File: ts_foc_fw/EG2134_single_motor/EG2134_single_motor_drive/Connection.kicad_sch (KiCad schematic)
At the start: 3 parts, among them CN1 XT30PW-M, CN2 WAFER-GH1.25-10PWB, U2 MR30PW-M30.G.Y

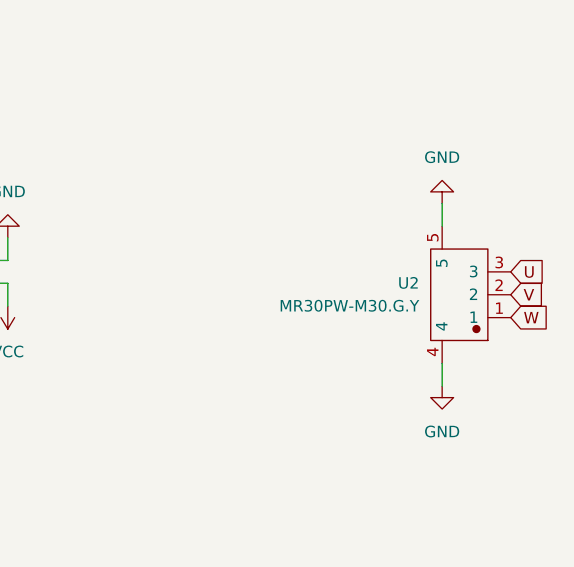
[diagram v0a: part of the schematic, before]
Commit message: PCB布局完成，等待布线
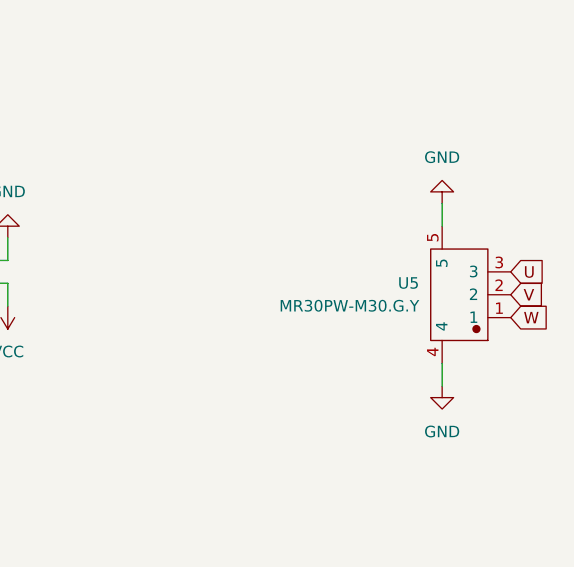
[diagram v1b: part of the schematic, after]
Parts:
- renumbered U2 to U5
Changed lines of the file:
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@@
 		(dnp no)
 		(fields_autoplaced yes)
-		(property "Reference" "#PWR09"
+		(property "Reference" "#PWR031"
 			(at 77.47 69.85 0)
 			(effects
@@
 			(project ""
 				(path "/a69a3027-f6f2-4dc7-8446-d1a07c691b27/9b51b494-1b93-4e31-bc4e-8becface2ca1"
-					(reference "#PWR09")
+					(reference "#PWR031")
 					(unit 1)
 				)
@@
 		(dnp no)
 		(fields_autoplaced yes)
-		(property "Reference" "#PWR017"
+		(property "Reference" "#PWR038"
 			(at 138.43 72.39 0)
 			(effects
@@
 			(project "EG2134_single_motor_drive"
 				(path "/a69a3027-f6f2-4dc7-8446-d1a07c691b27/9b51b494-1b93-4e31-bc4e-8becface2ca1"
-					(reference "#PWR017")
+					(reference "#PWR038")
 					(unit 1)
 				)
@@
 		(dnp no)
 		(fields_autoplaced yes)
-		(property "Reference" "#PWR015"
+		(property "Reference" "#PWR034"
 			(at 88.9 129.54 0)
 			(effects
@@
 			(project "EG2134_single_motor_drive"
 				(path "/a69a3027-f6f2-4dc7-8446-d1a07c691b27/9b51b494-1b93-4e31-bc4e-8becface2ca1"
-					(reference "#PWR015")
+					(reference "#PWR034")
 					(unit 1)
 				)
@@
 		(dnp no)
 		(fields_autoplaced yes)
-		(property "Reference" "#PWR013"
+		(property "Reference" "#PWR032"
 			(at 77.47 86.36 0)
 			(effects
@@
 			(project "EG2134_single_motor_drive"
 				(path "/a69a3027-f6f2-4dc7-8446-d1a07c691b27/9b51b494-1b93-4e31-bc4e-8becface2ca1"
-					(reference "#PWR013")
+					(reference "#PWR032")
 					(unit 1)
 				)
@@
 		(dnp no)
 		(fields_autoplaced yes)
-		(property "Reference" "#PWR011"
+		(property "Reference" "#PWR035"
 			(at 90.17 43.18 0)
 			(effects
@@
 			(project "EG2134_single_motor_drive"
 				(path "/a69a3027-f6f2-4dc7-8446-d1a07c691b27/9b51b494-1b93-4e31-bc4e-8becface2ca1"
-					(reference "#PWR011")
+					(reference "#PWR035")
 					(unit 1)
 				)
@@
 		(dnp no)
 		(fields_autoplaced yes)
-		(property "Reference" "#PWR014"
+		(property "Reference" "#PWR033"
 			(at 77.47 137.16 0)
 			(effects
@@
 			(project "EG2134_single_motor_drive"
 				(path "/a69a3027-f6f2-4dc7-8446-d1a07c691b27/9b51b494-1b93-4e31-bc4e-8becface2ca1"
-					(reference "#PWR014")
+					(reference "#PWR033")
 					(unit 1)
 				)
@@
 		(dnp no)
 		(fields_autoplaced yes)
-		(property "Reference" "#PWR012"
+		(property "Reference" "#PWR036"
 			(at 90.17 53.34 0)
 			(effects
@@
 			(project ""
 				(path "/a69a3027-f6f2-4dc7-8446-d1a07c691b27/9b51b494-1b93-4e31-bc4e-8becface2ca1"
-					(reference "#PWR012")
+					(reference "#PWR036")
 					(unit 1)
 				)
@@
 		(dnp no)
 		(fields_autoplaced yes)
-		(property "Reference" "U2"
+		(property "Reference" "U5"
 			(at 135.89 54.6099 0)
 			(effects
@@
 			(project ""
 				(path "/a69a3027-f6f2-4dc7-8446-d1a07c691b27/9b51b494-1b93-4e31-bc4e-8becface2ca1"
-					(reference "U2")
+					(reference "U5")
 					(unit 1)
 				)
@@
 		(dnp no)
 		(fields_autoplaced yes)
-		(property "Reference" "#PWR016"
+		(property "Reference" "#PWR037"
 			(at 138.43 39.37 0)
 			(effects
@@
 			(project "EG2134_single_motor_drive"
 				(path "/a69a3027-f6f2-4dc7-8446-d1a07c691b27/9b51b494-1b93-4e31-bc4e-8becface2ca1"
-					(reference "#PWR016")
+					(reference "#PWR037")
 					(unit 1)
 				)
@@
 		(dnp no)
 		(fields_autoplaced yes)
-		(property "Reference" "#PWR010"
+		(property "Reference" "#PWR030"
 			(at 77.47 38.1 0)
 			(effects
@@
 			(project "EG2134_single_motor_drive"
 				(path "/a69a3027-f6f2-4dc7-8446-d1a07c691b27/9b51b494-1b93-4e31-bc4e-8becface2ca1"
-					(reference "#PWR010")
-					(unit 1)
-				)
+					(reference "#PWR030")
+					(unit 1)
+				)

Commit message: tongbu
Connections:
- net CS_1 renamed CS1
- net CS_2 renamed CS2
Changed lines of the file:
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@@
+	(wire
+		(pts
+			(xy 90.17 100.33) (xy 86.36 100.33)
+		)
+		(stroke
+			(width 0)
+			(type default)
+		)
+	)
+	(wire
+		(pts
+			(xy 90.17 102.87) (xy 86.36 102.87)
+		)
+		(stroke
+			(width 0)
+			(type default)
+		)
+	)
 	(wire
 		(pts
@@
 	(wire
 		(pts
+			(xy 90.17 107.95) (xy 86.36 107.95)
+		)
+		(stroke
+			(width 0)
+			(type default)
+		)
+	)
+	(wire
+		(pts
+			(xy 90.17 110.49) (xy 86.36 110.49)
+		)
+		(stroke
+			(width 0)
+			(type default)
+		)
+	)
+	(wire
+		(pts
 			(xy 138.43 45.72) (xy 138.43 48.26)
 		)
@@
 		(pts
 			(xy 77.47 130.81) (xy 77.47 128.27)
+		)
+		(stroke
+			(width 0)
+			(type default)
+		)
+	)
+	(wire
+		(pts
+			(xy 90.17 105.41) (xy 86.36 105.41)
 		)
 		(stroke
@@
 		)
 	)
-	(global_label "CS_1"
-		(shape input)
-		(at 86.36 107.95 0)
-		(fields_autoplaced yes)
-		(effects
-			(font
-				(size 1.27 1.27)
-			)
-			(justify left)
-		)
-		(property "Intersheetrefs" "${INTERSHEET_REFS}"
-			(at 94.0018 107.95 0)
+	(global_label "CS1"
+		(shape input)
+		(at 90.17 107.95 0)
+		(fields_autoplaced yes)
+		(effects
+			(font
+				(size 1.27 1.27)
+			)
+			(justify left)
+		)
+		(property "Intersheetrefs" "${INTERSHEET_REFS}"
+			(at 96.8442 107.95 0)
 			(effects
 				(font
@@
 	(global_label "IN_2"
 		(shape input)
-		(at 86.36 102.87 0)
-		(fields_autoplaced yes)
-		(effects
-			(font
-				(size 1.27 1.27)
-			)
-			(justify left)
-		)
-		(property "Intersheetrefs" "${INTERSHEET_REFS}"
-			(at 93.4576 102.87 0)
-			(effects
-				(font
-					(size 1.27 1.27)
-				)
-				(justify left)
-				(hide yes)
-			)
-		)
-	)
-	(global_label "CS_2"
-		(shape input)
-		(at 86.36 110.49 0)
-		(fields_autoplaced yes)
-		(effects
-			(font
-				(size 1.27 1.27)
-			)
-			(justify left)
-		)
-		(property "Intersheetrefs" "${INTERSHEET_REFS}"
-			(at 94.0018 110.49 0)
+		(at 90.17 102.87 0)
+		(fields_autoplaced yes)
+		(effects
+			(font
+				(size 1.27 1.27)
+			)
+			(justify left)
+		)
+		(property "Intersheetrefs" "${INTERSHEET_REFS}"
+			(at 97.2676 102.87 0)
+			(effects
+				(font
+					(size 1.27 1.27)
+				)
+				(justify left)
+				(hide yes)
+			)
+		)
+	)
+	(global_label "CS2"
+		(shape input)
+		(at 90.17 110.49 0)
+		(fields_autoplaced yes)
+		(effects
+			(font
+				(size 1.27 1.27)
+			)
+			(justify left)
+		)
+		(property "Intersheetrefs" "${INTERSHEET_REFS}"
+			(at 96.8442 110.49 0)
 			(effects
 				(font
@@
 	(global_label "IN_3"
 		(shape input)
-		(at 86.36 105.41 0)
-		(fields_autoplaced yes)
-		(effects
-			(font
-				(size 1.27 1.27)
-			)
-			(justify left)
-		)
-		(property "Intersheetrefs" "${INTERSHEET_REFS}"
-			(at 93.4576 105.41 0)
+		(at 90.17 105.41 0)
+		(fields_autoplaced yes)
+		(effects
+			(font
+				(size 1.27 1.27)
+			)
+			(justify left)
+		)
+		(property "Intersheetrefs" "${INTERSHEET_REFS}"
+			(at 97.2676 105.41 0)
 			(effects
 				(font
@@
 	(global_label "IN_1"
 		(shape input)
-		(at 86.36 100.33 0)
-		(fields_autoplaced yes)
-		(effects
-			(font
-				(size 1.27 1.27)
-			)
-			(justify left)
-		)
-		(property "Intersheetrefs" "${INTERSHEET_REFS}"
-			(at 93.4576 100.33 0)
-			(effects
-				(font
+		(at 90.17 100.33 0)
+		(fields_autoplaced yes)
+		(effects
+			(font
+				(size 1.27 1.27)
+			)
+			(justify left)
+		)
+		(property "Intersheetrefs" "${INTERSHEET_REFS}"
+			(at 97.2676 100.33 0)
+			(effects
+				(font
